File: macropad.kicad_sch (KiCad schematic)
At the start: 22 parts, among them J1 SWD, SW10 Reset, U1 AP62250WU, U2 STM32F042K6Tx

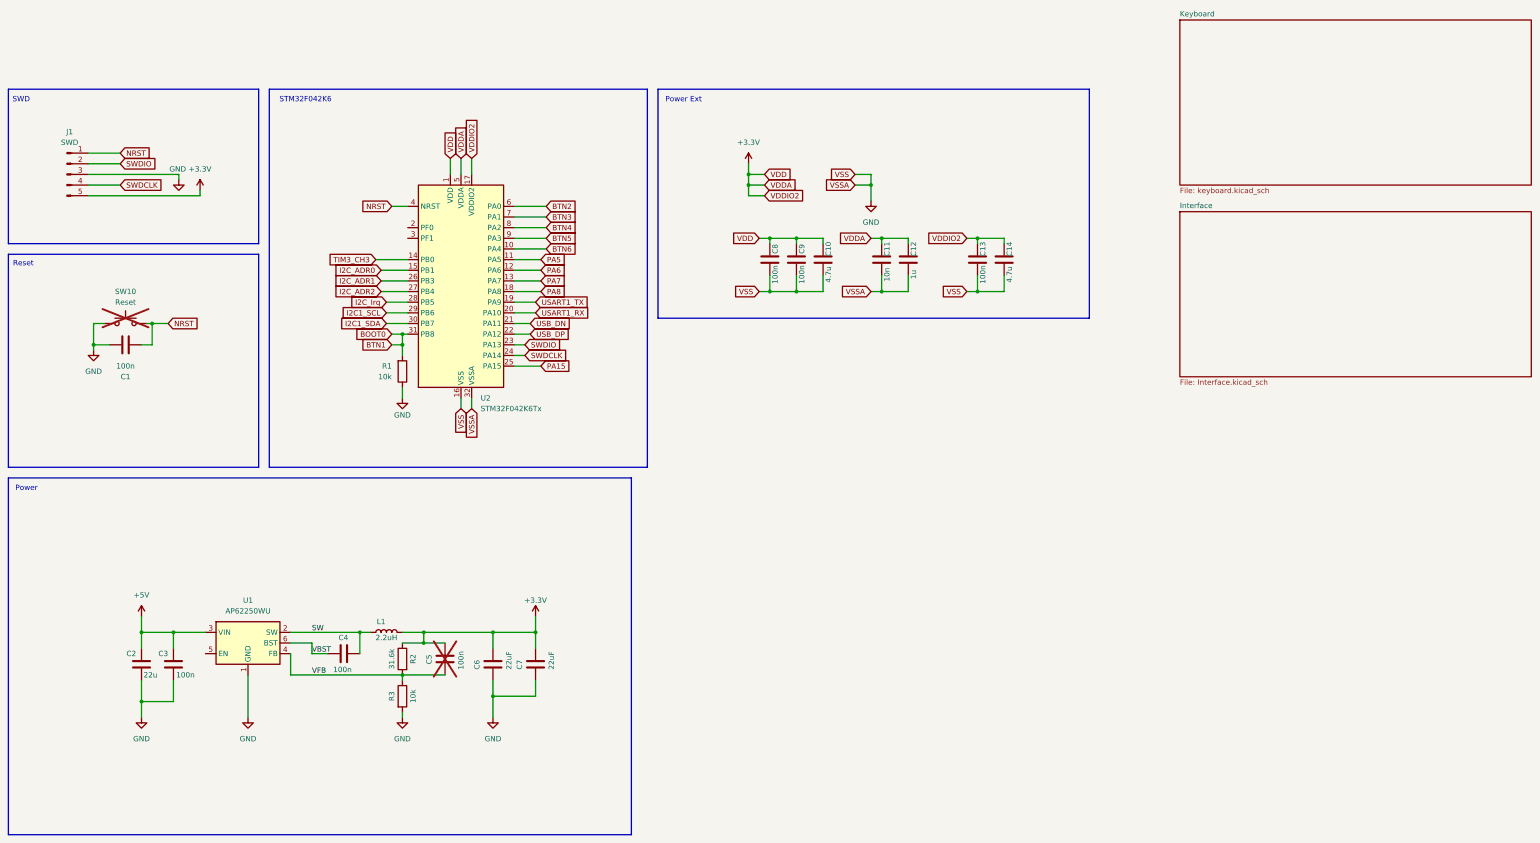
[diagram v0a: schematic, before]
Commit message: - Created head board tilable up to 4x - Placed and routed lines ToDo: - Print - I2C reanbable
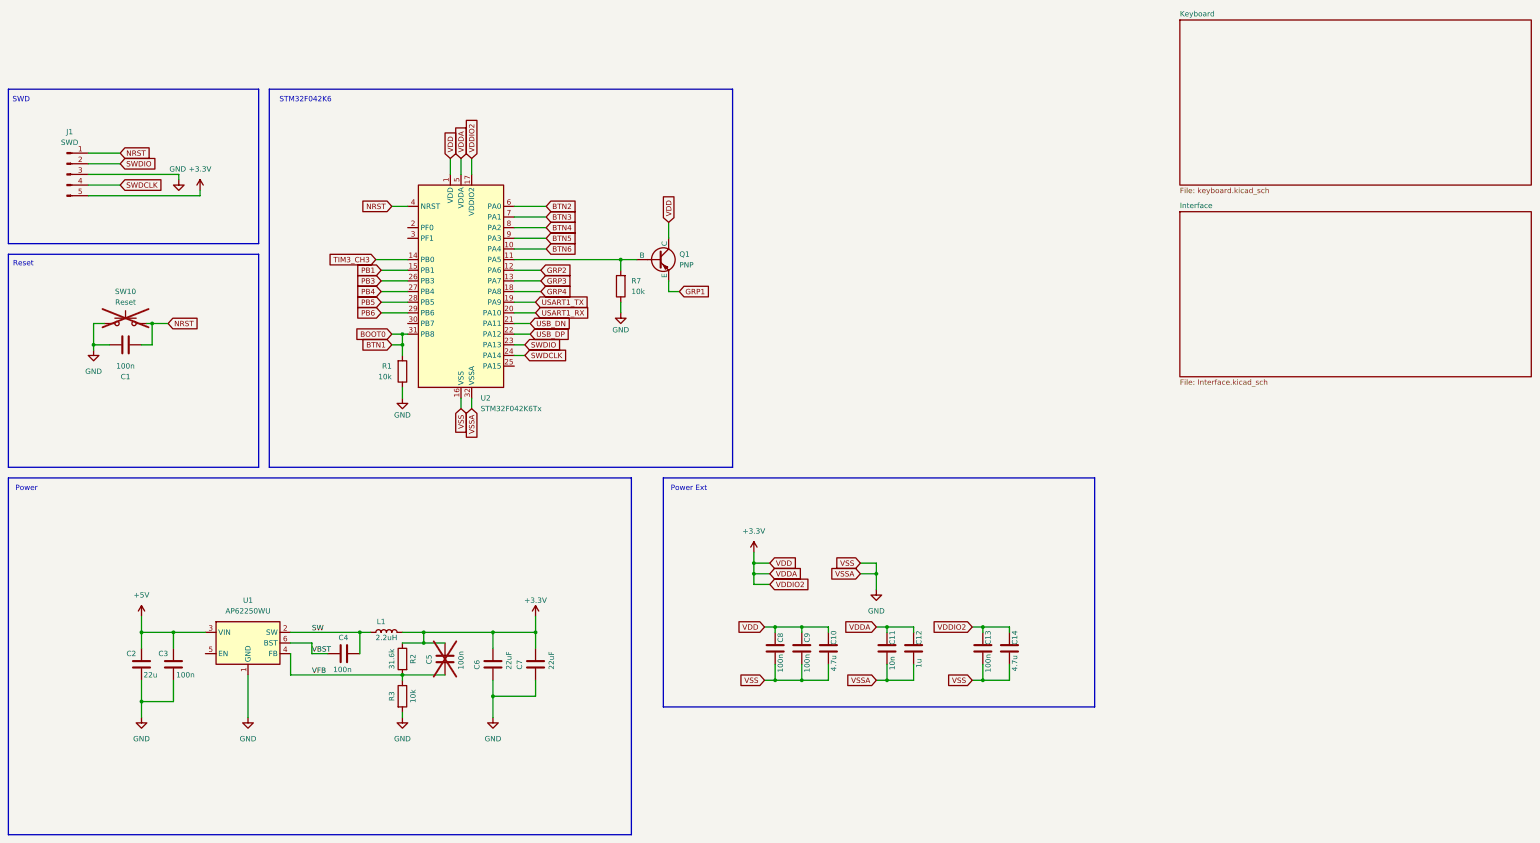
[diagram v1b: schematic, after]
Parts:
- added Q1: PNP, Package_TO_SOT_SMD:SOT-23, symbol Simulation_SPICE:PNP
- added R7: 10k, Resistor_SMD:R_0805_2012Metric_Pad1.20x1.40mm_HandSolder, symbol Device:R
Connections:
- net +3.3V: now also Q1.1 (C)
- net GND: now also R7.1
- net I2C1_SCL renamed PB6
- net I2C1_SDA: no longer names the net of U2.30 (PB7)
- net I2C_ADR0 renamed PB1
- net I2C_ADR1 renamed PB3
- net I2C_ADR2 renamed PB4
- net I2C_Irq renamed PB5
- net PA15: no longer names the net of U2.25 (PA15)
- net PA5: no longer names the net of U2.11 (PA5)
- net PA5: now also Q1.2 (B), R7.2
- net PA6 renamed GRP2
- net PA7 renamed GRP3
- net PA8 renamed GRP4
- new net GRP1: Q1.3 (E)
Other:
- moved on the sheet: C10, C11, C12, C13, C14, C8, C9

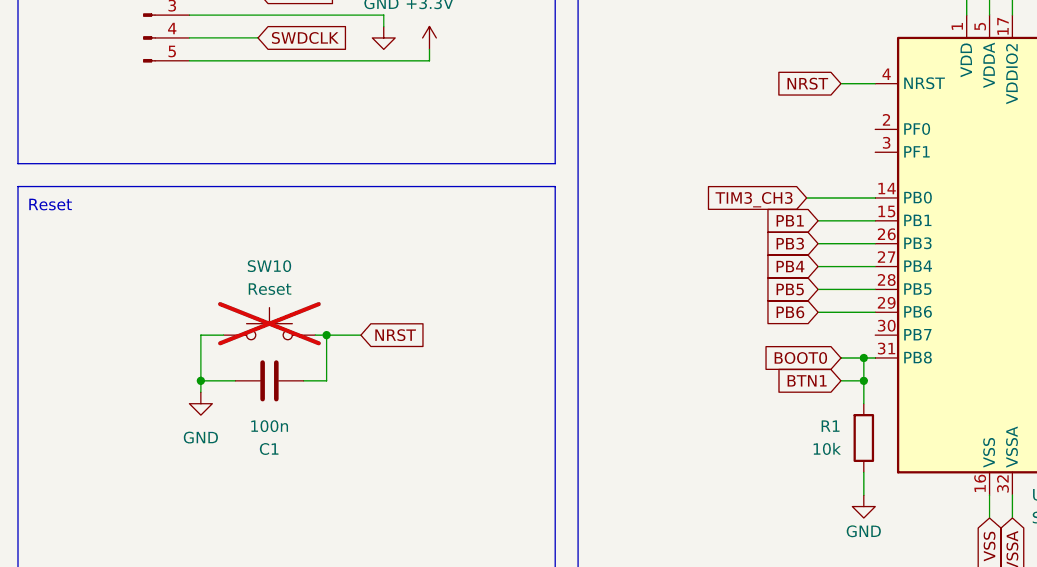
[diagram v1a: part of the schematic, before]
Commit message: - Added Pull Ups for I2C - Added second reset button on bottom side
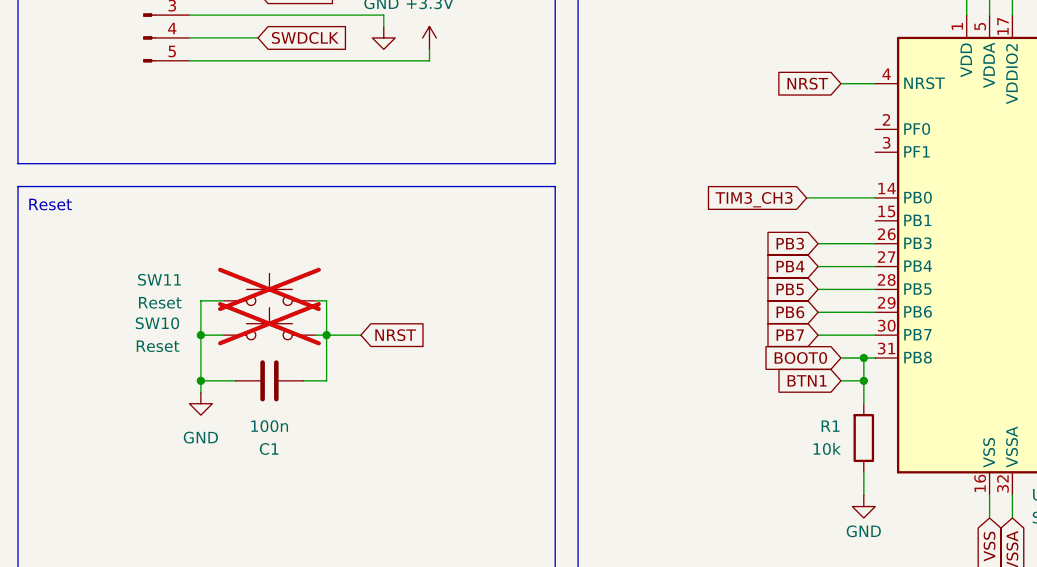
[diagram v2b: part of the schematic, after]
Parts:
- added SW11: Reset, Button_Switch_SMD:SW_SPST_B3U-1000P, symbol Switch:SW_Push
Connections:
- net GND: now also SW11.1
- net NRST: now also SW11.2
- net PB7: now reaches U2.30 (PB7)
- net PB1: no longer names the net of U2.15 (PB1)
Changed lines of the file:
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@@
 	)
 	(junction
+		(at 44.45 72.39)
+		(diameter 0)
+		(color 0 0 0 0)
+	)
+	(junction
 		(at 63.5 146.05)
 		(diameter 0)
@@
 	(wire
 		(pts
+			(xy 58.42 68.58) (xy 58.42 72.39)
+		)
+		(stroke
+			(width 0)
+			(type default)
+		)
+	)
+	(wire
+		(pts
 			(xy 144.78 69.85) (xy 149.86 69.85)
 		)
@@
 	(wire
 		(pts
-			(xy 113.03 59.69) (xy 119.38 59.69)
-		)
-		(stroke
-			(width 0)
-			(type default)
-		)
-	)
-	(wire
-		(pts
 			(xy 144.78 64.77) (xy 151.13 64.77)
 		)
@@
 	(wire
 		(pts
+			(xy 46.99 68.58) (xy 44.45 68.58)
+		)
+		(stroke
+			(width 0)
+			(type default)
+		)
+	)
+	(wire
+		(pts
 			(xy 240.03 144.78) (xy 240.03 146.05)
 		)
@@
 	(wire
 		(pts
+			(xy 57.15 68.58) (xy 58.42 68.58)
+		)
+		(stroke
+			(width 0)
+			(type default)
+		)
+	)
+	(wire
+		(pts
 			(xy 144.78 80.01) (xy 147.32 80.01)
 		)
@@
 	(wire
 		(pts
+			(xy 113.03 72.39) (xy 119.38 72.39)
+		)
+		(stroke
+			(width 0)
+			(type default)
+		)
+	)
+	(wire
+		(pts
 			(xy 55.88 142.24) (xy 55.88 146.05)
 		)
@@
 	(wire
 		(pts
+			(xy 44.45 68.58) (xy 44.45 72.39)
+		)
+		(stroke
+			(width 0)
+			(type default)
+		)
+	)
+	(wire
+		(pts
 			(xy 149.86 146.05) (xy 139.7 146.05)
 		)
@@
 		)
 	)
+	(global_label "PB7"
+		(shape input)
+		(at 113.03 72.39 180)
+		(fields_autoplaced yes)
+		(effects
+			(font
+				(size 1.27 1.27)
+			)
+			(justify right)
+		)
+		(property "Intersheetrefs" "${INTERSHEET_REFS}"
+			(at 106.2953 72.39 0)
+			(effects
+				(font
+					(size 1.27 1.27)
+				)
+				(justify right)
+				(hide yes)
+			)
+		)
+	)
 	(global_label "USB_DN"
 		(shape input)
@@
 		)
 	)
-	(global_label "PB1"
-		(shape input)
-		(at 113.03 59.69 180)
-		(fields_autoplaced yes)
-		(effects
-			(font
-				(size 1.27 1.27)
-			)
-			(justify right)
-		)
-		(property "Intersheetrefs" "${INTERSHEET_REFS}"
-			(at 106.2953 59.69 0)
-			(effects
-				(font
-					(size 1.27 1.27)
-				)
-				(justify right)
-				(hide yes)
-			)
-		)
-	)
 	(global_label "VSS"
 		(shape input)
@@
 		(on_board yes)
 		(dnp yes)
-		(fields_autoplaced yes)
 		(property "Reference" "SW10"
-			(at 52.07 64.77 0)
+			(at 39.624 71.12 0)
 			(effects
 				(font
@@
 		)
 		(property "Value" "Reset"
-			(at 52.07 67.31 0)
+			(at 39.624 73.66 0)
 			(effects
 				(font
@@
 					(unit 1)
 				)
+			)
+		)
+	)
+	(symbol
+		(lib_id "Switch:SW_Push")
+		(at 52.07 68.58 0)
+		(unit 1)
+		(exclude_from_sim no)
+		(in_bom yes)
+		(on_board yes)
+		(dnp yes)
+		(property "Reference" "SW11"
+			(at 39.878 66.294 0)
+			(effects
+				(font
+					(size 1.27 1.27)
+				)
+			)
+		)
+		(property "Value" "Reset"
+			(at 39.878 68.834 0)
+			(effects
+				(font
+					(size 1.27 1.27)
+				)
+			)
+		)
+		(property "Footprint" "Button_Switch_SMD:SW_SPST_B3U-1000P"
+			(at 52.07 63.5 0)
+			(effects
+				(font
+					(size 1.27 1.27)
+				)
+				(hide yes)
+			)
+		)
+		(property "Datasheet" "~"
+			(at 52.07 63.5 0)
+			(effects
+				(font
+					(size 1.27 1.27)
+				)
+				(hide yes)
+			)
+		)
+		(property "Description" "Push button switch, generic, two pins"
+			(at 52.07 68.58 0)
+			(effects
+				(font
+					(size 1.27 1.27)
+				)
+				(hide yes)
+			)
+		)
+		(pin "2"
+		)
+		(pin "1"
+		)
+		(instances
+			(project "macropad"
+				(path "/affdcae3-2b9b-4248-bf2d-36ec8abc82bb"
+					(reference "SW11")
+					(unit 1)
+				)

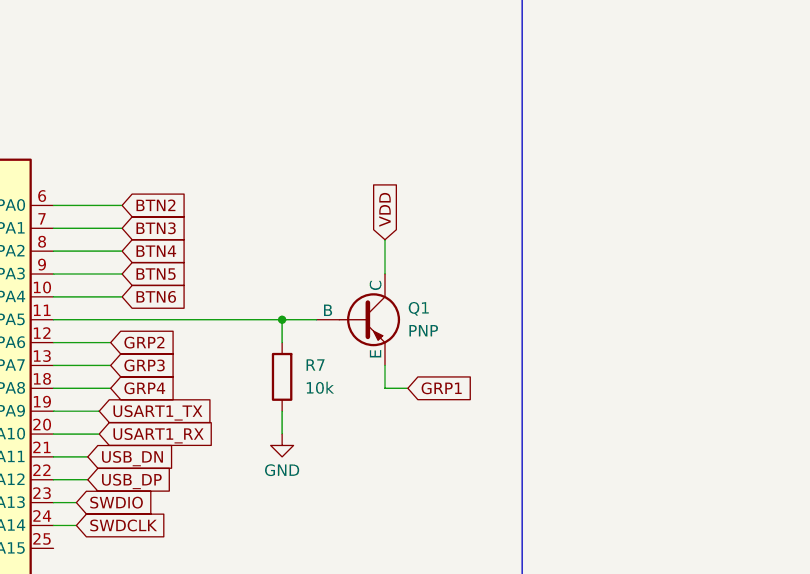
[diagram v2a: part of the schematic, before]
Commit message: - fixed error in transistor circuit - fixed orientation of silkscreen text - DRC: Okay
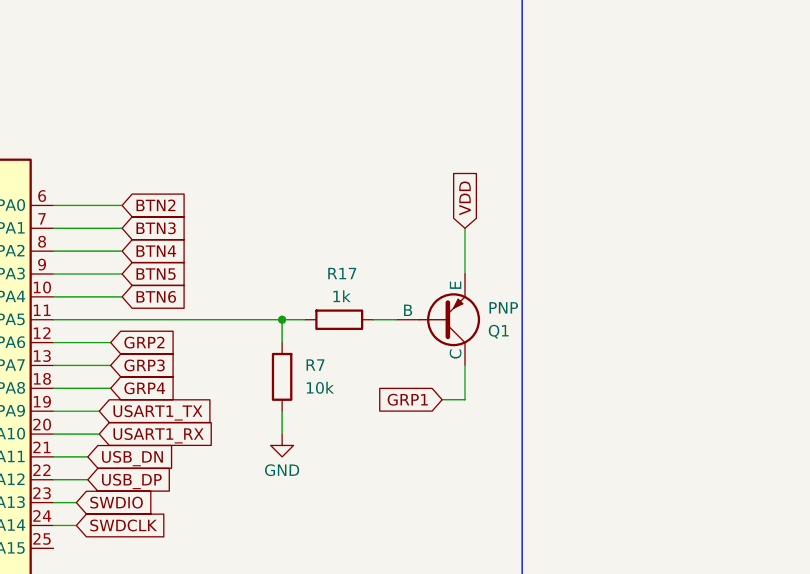
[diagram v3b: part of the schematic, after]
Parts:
- added R17: 1k, Resistor_SMD:R_0805_2012Metric_Pad1.20x1.40mm_HandSolder, symbol Device:R
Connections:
- net +3.3V: now also Q1.3 (E); no longer Q1.1 (C)
- net GRP1: now also Q1.1 (C); no longer Q1.3 (E)
- net at R7.2, U2.11 (PA5): now also R17.2; no longer Q1.2 (B)
- new net: Q1.2 (B), R17.1
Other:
- moved on the sheet: Q1
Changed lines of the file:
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@@
 	(wire
 		(pts
-			(xy 181.61 62.23) (xy 181.61 64.77)
+			(xy 190.5 62.23) (xy 190.5 66.04)
 		)
 		(stroke
@@
 	(wire
 		(pts
-			(xy 181.61 48.26) (xy 181.61 52.07)
+			(xy 190.5 46.99) (xy 190.5 52.07)
 		)
 		(stroke
@@
 	(wire
 		(pts
-			(xy 170.18 57.15) (xy 173.99 57.15)
+			(xy 170.18 57.15) (xy 172.72 57.15)
 		)
 		(stroke
@@
 	(wire
 		(pts
-			(xy 181.61 64.77) (xy 184.15 64.77)
+			(xy 190.5 66.04) (xy 187.96 66.04)
 		)
 		(stroke
@@
 	(wire
 		(pts
+			(xy 180.34 57.15) (xy 182.88 57.15)
+		)
+		(stroke
+			(width 0)
+			(type default)
+		)
+	)
+	(wire
+		(pts
 			(xy 55.88 146.05) (xy 55.88 149.86)
 		)
@@
 	(global_label "VDD"
 		(shape input)
-		(at 181.61 48.26 90)
+		(at 190.5 46.99 90)
 		(fields_autoplaced yes)
 		(effects
@@
 		)
 		(property "Intersheetrefs" "${INTERSHEET_REFS}"
-			(at 181.61 41.6462 90)
+			(at 190.5 40.3762 90)
 			(effects
 				(font
@@
 	(global_label "GRP1"
 		(shape input)
-		(at 184.15 64.77 0)
+		(at 187.96 66.04 180)
 		(fields_autoplaced yes)
 		(effects
@@
 				(size 1.27 1.27)
 			)
-			(justify left)
+			(justify right)
 		)
 		(property "Intersheetrefs" "${INTERSHEET_REFS}"
-			(at 192.1547 64.77 0)
+			(at 179.9553 66.04 0)
 			(effects
 				(font
 					(size 1.27 1.27)
 				)
-				(justify left)
+				(justify right)
 				(hide yes)
 			)
@@
 	(symbol
 		(lib_id "Simulation_SPICE:PNP")
-		(at 179.07 57.15 0)
+		(at 187.96 57.15 0)
+		(mirror x)
 		(unit 1)
 		(exclude_from_sim no)
@@
 		(on_board yes)
 		(dnp no)
-		(fields_autoplaced yes)
 		(property "Reference" "Q1"
-			(at 184.15 55.8799 0)
+			(at 193.04 58.4201 0)
 			(effects
 				(font
@@
 		)
 		(property "Value" "PNP"
-			(at 184.15 58.4199 0)
+			(at 193.04 55.8801 0)
 			(effects
 				(font
@@
 		)
 		(property "Footprint" "Package_TO_SOT_SMD:SOT-23"
-			(at 214.63 57.15 0)
+			(at 223.52 57.15 0)
 			(effects
 				(font
@@
 		)
 		(property "Datasheet" "https://ngspice.sourceforge.io/docs/ngspice-html-manual/manual.xhtml#cha_BJTs"
-			(at 214.63 57.15 0)
+			(at 223.52 57.15 0)
 			(effects
 				(font
@@
 		)
 		(property "Description" "Bipolar transistor symbol for simulation only, substrate tied to the emitter"
-			(at 179.07 57.15 0)
+			(at 187.96 57.15 0)
 			(effects
 				(font
@@
 		)
 		(property "Sim.Device" "PNP"
-			(at 179.07 57.15 0)
+			(at 187.96 57.15 0)
 			(effects
 				(font
@@
 		)
 		(property "Sim.Type" "GUMMELPOON"
-			(at 179.07 57.15 0)
+			(at 187.96 57.15 0)
 			(effects
 				(font
@@
 		)
 		(property "Sim.Pins" "1=C 2=B 3=E"
-			(at 179.07 57.15 0)
+			(at 187.96 57.15 0)
 			(effects
 				(font
@@
 					(unit 1)
 				)
+			)
+		)
+	)
+	(symbol
+		(lib_id "Device:R")
+		(at 176.53 57.15 270)
+		(unit 1)
+		(exclude_from_sim no)
+		(in_bom yes)
+		(on_board yes)
+		(dnp no)
+		(property "Reference" "R17"
+			(at 178.562 52.07 90)
+			(effects
+				(font
+					(size 1.27 1.27)
+				)
+				(justify right)
+			)
+		)
+		(property "Value" "1k"
+			(at 177.7999 54.61 90)
+			(effects
+				(font
+					(size 1.27 1.27)
+				)
+				(justify right)
+			)
+		)
+		(property "Footprint" "Resistor_SMD:R_0805_2012Metric_Pad1.20x1.40mm_HandSolder"
+			(at 176.53 55.372 90)
+			(effects
+				(font
+					(size 1.27 1.27)
+				)
+				(hide yes)
+			)
+		)
+		(property "Datasheet" "~"
+			(at 176.53 57.15 0)
+			(effects
+				(font
+					(size 1.27 1.27)
+				)
+				(hide yes)
+			)
+		)
+		(property "Description" "Resistor"
+			(at 176.53 57.15 0)
+			(effects
+				(font
+					(size 1.27 1.27)
+				)
+				(hide yes)
+			)
+		)
+		(pin "1"
+		)
+		(pin "2"
+		)
+		(instances
+			(project "macropad"
+				(path "/affdcae3-2b9b-4248-bf2d-36ec8abc82bb"
+					(reference "R17")
+					(unit 1)
+				)

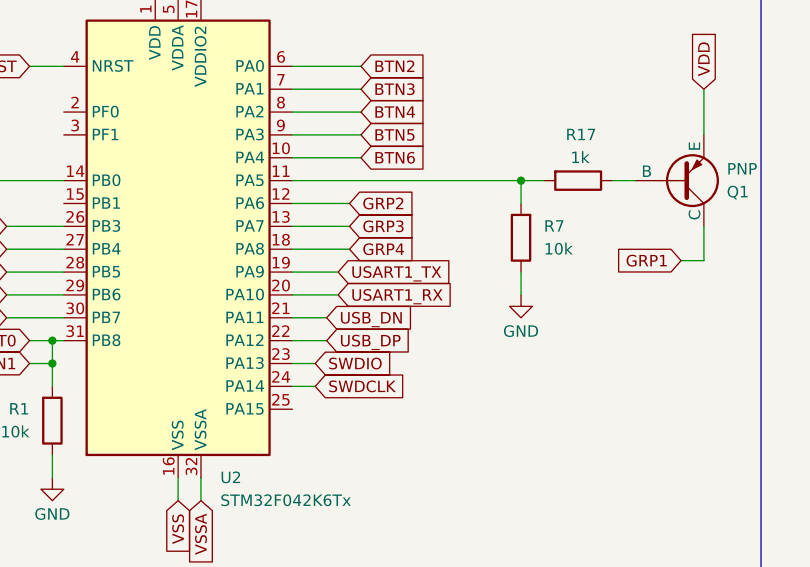
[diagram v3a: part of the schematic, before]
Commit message: - Added missing library files to git - Added logo to silkscreen - ERC: Okay
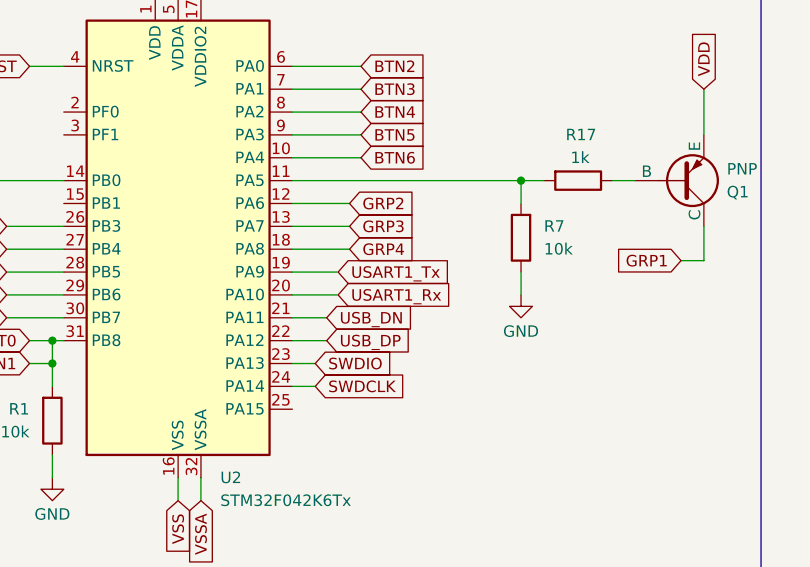
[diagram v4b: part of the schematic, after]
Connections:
- net USART1_RX renamed USART1_Rx
- net USART1_TX renamed USART1_Tx
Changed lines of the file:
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@@
 		)
 	)
-	(global_label "USART1_RX"
+	(global_label "USART1_Rx"
 		(shape input)
 		(at 149.86 69.85 0)
@@
 		)
 	)
-	(global_label "USART1_TX"
+	(global_label "USART1_Tx"
 		(shape input)
 		(at 149.86 67.31 0)
